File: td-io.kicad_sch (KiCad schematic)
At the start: 12 parts, among them J1 Conn_01x04, J2 USB_B, J3 Conn_01x02, J4 Conn_01x02, Q1 AO4818B, U12 CPC1017N, U2 ISL3175EIBZ-T

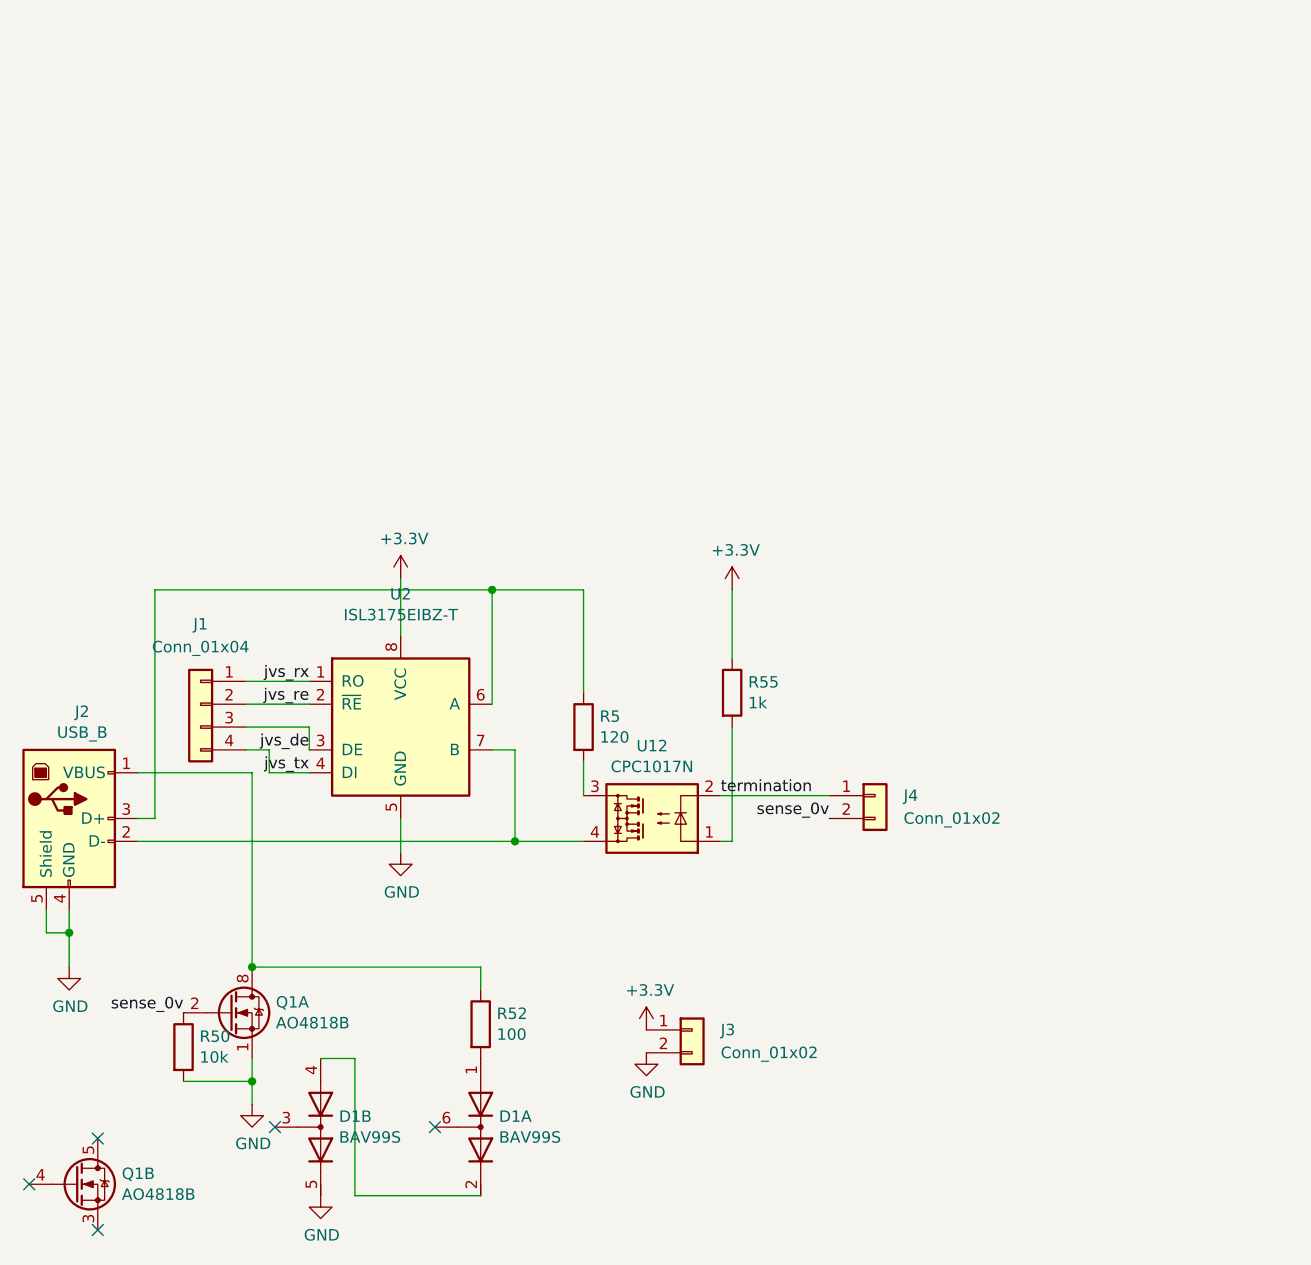
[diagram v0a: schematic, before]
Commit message: Updated pcb with onboard pico
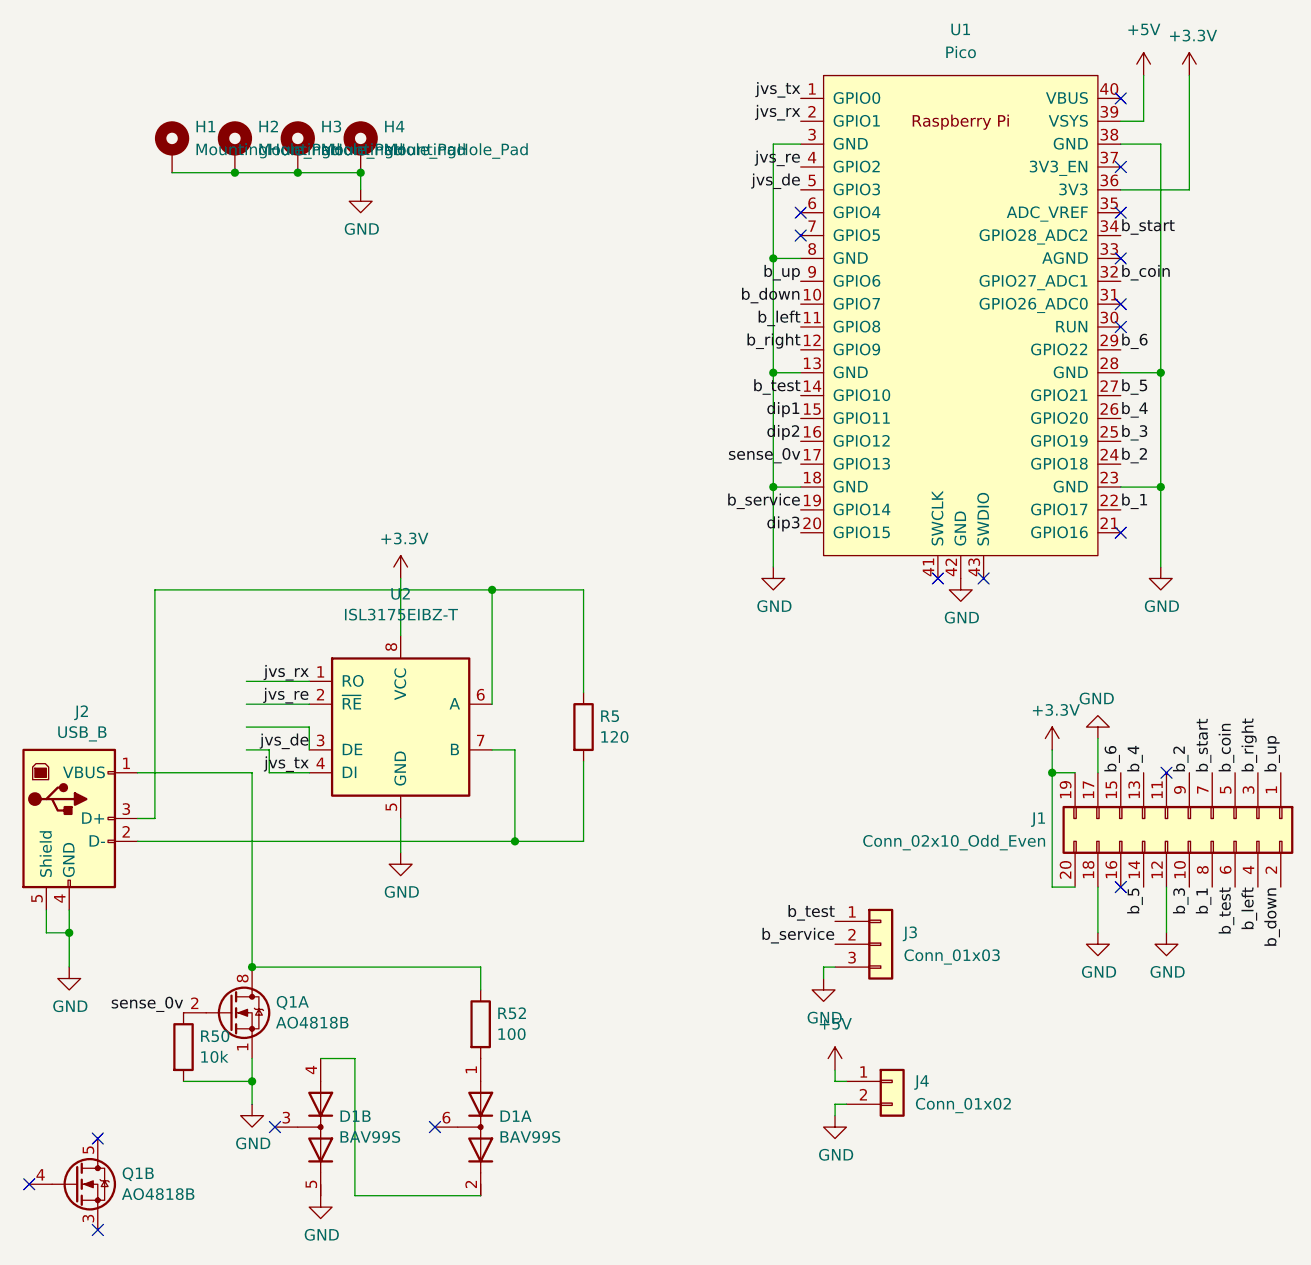
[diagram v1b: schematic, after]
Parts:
- removed J1: Conn_01x04, Connector_PinHeader_2.54mm:PinHeader_1x04_P2.54mm_Vertical, symbol Connector_Generic:Conn_01x04
- removed J3: Conn_01x02, Connector_PinHeader_2.54mm:PinHeader_1x02_P2.54mm_Vertical, symbol Connector_Generic:Conn_01x02
- removed R55: 1k, Resistor_SMD:R_0805_2012Metric, symbol Device:R
- removed U12: CPC1017N, Package_SO:SOP-4_3.8x4.1mm_P2.54mm, symbol Relay_SolidState:CPC1017N
- added H1, H2, H3, H4: MountingHole_Pad, MountingHole:MountingHole_3.5mm_Pad, symbol Mechanical:MountingHole_Pad
- added J1: Conn_02x10_Odd_Even, Connector_PinHeader_2.54mm:PinHeader_2x10_P2.54mm_Vertical, symbol Connector_Generic:Conn_02x10_Odd_Even
- added J3: Conn_01x03, Connector_PinHeader_2.54mm:PinHeader_1x03_P2.54mm_Vertical, symbol Connector_Generic:Conn_01x03
- added U1: Pico, RPi_Pico:RPi_Pico_SMD_TH, symbol MCU_RaspberryPi_and_Boards:Pico
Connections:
- net +3V3: now also J1.19 (Pin_19), J1.20 (Pin_20), U1.36 (3V3)
- net GND: now also J4.2 (Pin_2), H1.1, H2.1, H3.1, H4.1, J1.12 (Pin_12), J1.17 (Pin_17), J1.18 (Pin_18), J3.3 (Pin_3), U1.13 (GND), U1.18 (GND), U1.23 (GND), U1.28 (GND), U1.3 (GND), U1.38 (GND), U1.42 (GND), U1.8 (GND)
- net jvs_de: now also U1.5 (GPIO3)
- net jvs_re: now also U1.4 (GPIO2)
- net jvs_rx: now also U1.2 (GPIO1)
- net jvs_tx: now also U1.1 (GPIO0)
- net sense_0v: now also U1.17 (GPIO13); no longer J4.2 (Pin_2)
- net at J2.2 (D-), U2.7 (B): now also R5.2
- net termination renamed +5V
- net +5V: now also U1.39 (VSYS)
- new net b_1: J1.8 (Pin_8), U1.22 (GPIO17)
- new net b_2: J1.9 (Pin_9), U1.24 (GPIO18)
- new net b_3: J1.10 (Pin_10), U1.25 (GPIO19)
- new net b_4: J1.13 (Pin_13), U1.26 (GPIO20)
- new net b_5: J1.14 (Pin_14), U1.27 (GPIO21)
- new net b_6: J1.15 (Pin_15), U1.29 (GPIO22)
- new net b_coin: J1.5 (Pin_5), U1.32 (GPIO27_ADC1)
- new net b_down: J1.2 (Pin_2), U1.10 (GPIO7)
- new net b_left: J1.4 (Pin_4), U1.11 (GPIO8)
- new net b_right: J1.3 (Pin_3), U1.12 (GPIO9)
- new net b_service: J3.2 (Pin_2), U1.19 (GPIO14)
- new net b_start: J1.7 (Pin_7), U1.34 (GPIO28_ADC2)
- new net b_test: J1.6 (Pin_6), J3.1 (Pin_1), U1.14 (GPIO10)
- new net b_up: J1.1 (Pin_1), U1.9 (GPIO6)
- new net dip1: U1.15 (GPIO11)
- new net dip2: U1.16 (GPIO12)
- new net dip3: U1.20 (GPIO15)
- no-connect marks 5 -> 18

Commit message: Add some breakout pins
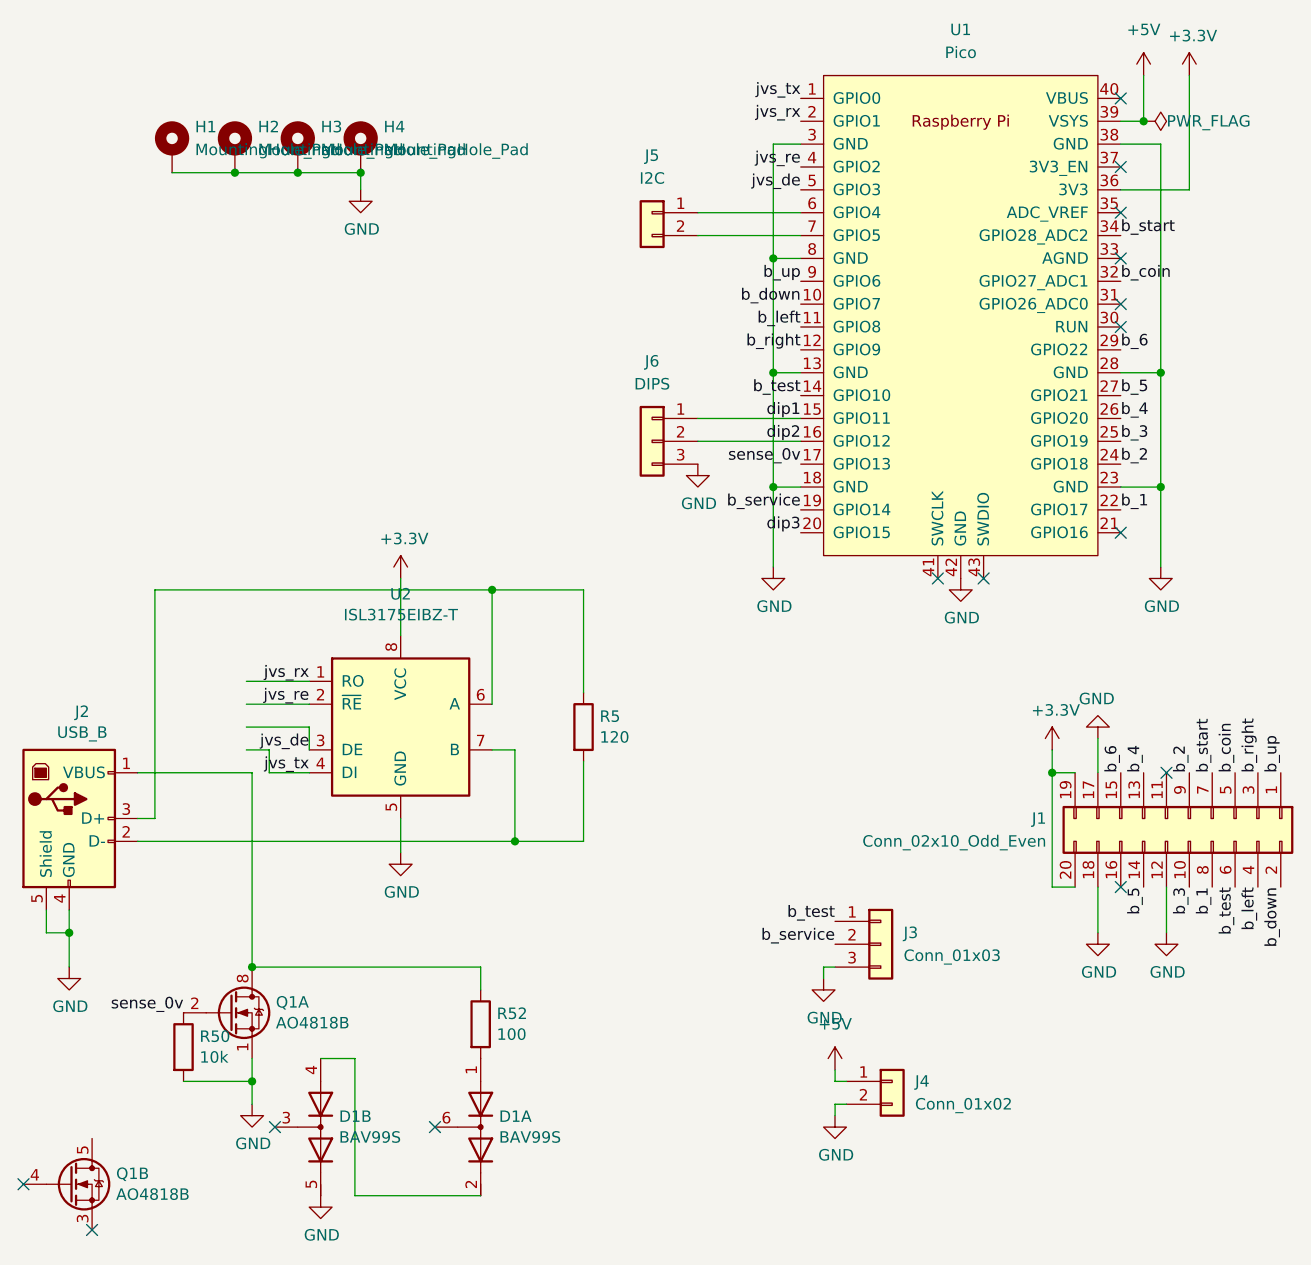
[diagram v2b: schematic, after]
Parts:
- added J5: I2C, Connector_PinHeader_2.54mm:PinHeader_1x02_P2.54mm_Vertical, symbol Connector_Generic:Conn_01x02
- added J6: DIPS, Connector_PinHeader_2.54mm:PinHeader_1x03_P2.54mm_Vertical, symbol Connector_Generic:Conn_01x03
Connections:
- net GND: now also J6.3 (Pin_3)
- net dip1: now also J6.1 (Pin_1)
- net dip2: now also J6.2 (Pin_2)
- net at U1.6 (GPIO4): now also J5.1 (Pin_1)
- net at U1.7 (GPIO5): now also J5.2 (Pin_2)
- no-connect marks 18 -> 15
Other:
- moved on the sheet: Q1B
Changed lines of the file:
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@@
   (junction (at 264.795 88.265) (diameter 0) (color 0 0 0 0)
+  )
+  (junction (at 365.76 82.55) (diameter 0) (color 0 0 0 0)
   )
   (junction (at 367.665 123.19) (diameter 0) (color 0 0 0 0)
@@
   (no_connect (at 269.24 194.31))
   (no_connect (at 363.22 102.87))
-  (no_connect (at 241.935 200.66))
-  (no_connect (at 249.555 205.74))
+  (no_connect (at 241.3 200.66))
+  (no_connect (at 248.92 205.74))
   (no_connect (at 347.98 133.35))
   (no_connect (at 342.9 133.35))
-  (no_connect (at 249.555 195.58))
   (no_connect (at 363.22 128.27))
-  (no_connect (at 327.66 95.25))
-  (no_connect (at 327.66 92.71))
   (wire (pts (xy 283.21 160.02) (xy 283.21 163.83))
     (stroke (width 0) (type default) (color 0 0 0 0))
   )
+  (wire (pts (xy 316.23 115.57) (xy 327.66 115.57))
+    (stroke (width 0) (type default) (color 0 0 0 0))
+  )
   (wire (pts (xy 292.1 176.53) (xy 292.1 179.07))
     (stroke (width 0) (type default) (color 0 0 0 0))
@@
     (stroke (width 0) (type default) (color 0 0 0 0))
   )
+  (wire (pts (xy 316.23 95.25) (xy 327.66 95.25))
+    (stroke (width 0) (type default) (color 0 0 0 0))
+  )
   (wire (pts (xy 332.74 191.77) (xy 331.47 191.77))
     (stroke (width 0) (type default) (color 0 0 0 0))
   )
+  (wire (pts (xy 316.23 118.11) (xy 327.66 118.11))
+    (stroke (width 0) (type default) (color 0 0 0 0))
+  )
   (wire (pts (xy 243.84 170.18) (xy 243.84 172.72))
     (stroke (width 0) (type default) (color 0 0 0 0))
@@
   )
   (wire (pts (xy 278.13 186.69) (xy 274.32 186.69))
+    (stroke (width 0) (type default) (color 0 0 0 0))
+  )
+  (wire (pts (xy 316.23 92.71) (xy 327.66 92.71))
     (stroke (width 0) (type default) (color 0 0 0 0))
   )
@@
     (pin "1")
   )
-  (symbol (lib_id "Transistor_FET:FDS6930B") (at 247.015 200.66 0) (unit 2)
-    (in_bom yes) (on_board yes)
-    (property "Reference" "Q1" (id 0) (at 252.222 199.4916 0)
-      (effects (font (size 1.27 1.27)) (justify left))
-    )
-    (property "Value" "AO4818B" (id 1) (at 252.222 201.803 0)
-      (effects (font (size 1.27 1.27)) (justify left))
-    )
-    (property "Footprint" "Package_SO:SOIC-8_3.9x4.9mm_P1.27mm" (id 2) (at 252.095 202.565 0)
+  (symbol (lib_id "Transistor_FET:FDS6930B") (at 246.38 200.66 0) (unit 2)
+    (in_bom yes) (on_board yes)
+    (property "Reference" "Q1" (id 0) (at 251.587 199.4916 0)
+      (effects (font (size 1.27 1.27)) (justify left))
+    )
+    (property "Value" "AO4818B" (id 1) (at 251.587 201.803 0)
+      (effects (font (size 1.27 1.27)) (justify left))
+    )
+    (property "Footprint" "Package_SO:SOIC-8_3.9x4.9mm_P1.27mm" (id 2) (at 251.46 202.565 0)
       (effects (font (size 1.27 1.27) italic) (justify left) hide)
     )
-    (property "Datasheet" "http://www.onsemi.com/pub/Collateral/FDS6930B-D.PDF" (id 3) (at 247.015 200.66 0)
+    (property "Datasheet" "http://www.onsemi.com/pub/Collateral/FDS6930B-D.PDF" (id 3) (at 246.38 200.66 0)
       (effects (font (size 1.27 1.27)) (justify left) hide)
     )
-    (property "Digikey" "785-1059-1-ND" (id 4) (at 247.015 200.66 0)
+    (property "Digikey" "785-1059-1-ND" (id 4) (at 246.38 200.66 0)
       (effects (font (size 1.27 1.27)) hide)
     )
@@
     )
     (pin "1")
+  )
+  (symbol (lib_id "Connector_Generic:Conn_01x03") (at 311.15 118.11 0) (mirror y) (unit 1)
+    (in_bom yes) (on_board yes) (fields_autoplaced)
+    (property "Reference" "J6" (id 0) (at 311.15 109.22 0))
+    (property "Value" "DIPS" (id 1) (at 311.15 111.76 0))
+    (property "Footprint" "Connector_PinHeader_2.54mm:PinHeader_1x03_P2.54mm_Vertical" (id 2) (at 311.15 118.11 0)
+      (effects (font (size 1.27 1.27)) hide)
+    )
+    (property "Datasheet" "~" (id 3) (at 311.15 118.11 0)
+      (effects (font (size 1.27 1.27)) hide)
+    )
+    (pin "1")
+    (pin "2")
+    (pin "3")
   )
   (symbol (lib_id "power:GND") (at 324.612 132.08 0) (unit 1)
@@
     (pin "1")
   )
+  (symbol (lib_id "power:GND") (at 316.23 120.65 0) (unit 1)
+    (in_bom yes) (on_board yes)
+    (property "Reference" "#PWR0117" (id 0) (at 316.23 127 0)
+      (effects (font (size 1.27 1.27)) hide)
+    )
+    (property "Value" "GND" (id 1) (at 316.357 125.0442 0))
+    (property "Footprint" "" (id 2) (at 316.23 120.65 0)
+      (effects (font (size 1.27 1.27)) hide)
+    )
+    (property "Datasheet" "" (id 3) (at 316.23 120.65 0)
+      (effects (font (size 1.27 1.27)) hide)
+    )
+    (pin "1")
+  )
   (symbol (lib_id "Connector_Generic:Conn_01x03") (at 336.55 173.99 0) (unit 1)
     (in_bom yes) (on_board yes) (fields_autoplaced)
@@
     )
     (property "Datasheet" "~" (id 3) (at 264.795 85.725 0)
+      (effects (font (size 1.27 1.27)) hide)
+    )
+    (pin "1")
+  )
+  (symbol (lib_id "power:PWR_FLAG") (at 365.76 82.55 270) (unit 1)
+    (in_bom yes) (on_board yes)
+    (property "Reference" "#FLG0101" (id 0) (at 367.665 82.55 0)
+      (effects (font (size 1.27 1.27)) hide)
+    )
+    (property "Value" "PWR_FLAG" (id 1) (at 368.3 82.55 90)
+      (effects (font (size 1.27 1.27)) (justify left))
+    )
+    (property "Footprint" "" (id 2) (at 365.76 82.55 0)
+      (effects (font (size 1.27 1.27)) hide)
+    )
+    (property "Datasheet" "~" (id 3) (at 365.76 82.55 0)
       (effects (font (size 1.27 1.27)) hide)
     )
@@
     (pin "9")
   )
+  (symbol (lib_id "Connector_Generic:Conn_01x02") (at 311.15 92.71 0) (mirror y) (unit 1)
+    (in_bom yes) (on_board yes) (fields_autoplaced)
+    (property "Reference" "J5" (id 0) (at 311.15 86.36 0))
+    (property "Value" "I2C" (id 1) (at 311.15 88.9 0))
+    (property "Footprint" "Connector_PinHeader_2.54mm:PinHeader_1x02_P2.54mm_Vertical" (id 2) (at 311.15 92.71 0)
+      (effects (font (size 1.27 1.27)) hide)
+    )
+    (property "Datasheet" "~" (id 3) (at 311.15 92.71 0)
+      (effects (font (size 1.27 1.27)) hide)
+    )
+    (pin "1")
+    (pin "2")
+  )
   (symbol (lib_id "Connector_Generic:Conn_01x02") (at 337.82 189.23 0) (unit 1)
     (in_bom yes) (on_board yes) (fields_autoplaced)
@@
   )
   (symbol_instances
+    (path "/b452654c-0af9-452a-9138-4303c0e3ebb7"
+      (reference "#FLG0101") (unit 1) (value "PWR_FLAG") (footprint "")
+    )
     (path "/0e2f4b55-afcf-4e5f-9559-8b2ad2098638"
       (reference "#PWR0101") (unit 1) (value "GND") (footprint "")
@@
       (reference "#PWR0116") (unit 1) (value "GND") (footprint "")
     )
+    (path "/887d0669-7224-46c3-b959-0cacd5c8d6af"
+      (reference "#PWR0117") (unit 1) (value "GND") (footprint "")
+    )
     (path "/00000000-0000-0000-0000-0000610da9f2"
       (reference "#PWR0139") (unit 1) (value "GND") (footprint "")
@@
       (reference "J4") (unit 1) (value "Conn_01x02") (footprint "Connector_PinHeader_2.54mm:PinHeader_1x02_P2.54mm_Vertical")
     )
+    (path "/be813dec-c91f-4c06-808b-c742fd6baf99"
+      (reference "J5") (unit 1) (value "I2C") (footprint "Connector_PinHeader_2.54mm:PinHeader_1x02_P2.54mm_Vertical")
+    )
+    (path "/37ca6a20-f162-4f7d-b75b-aebcef62a374"
+      (reference "J6") (unit 1) (value "DIPS") (footprint "Connector_PinHeader_2.54mm:PinHeader_1x03_P2.54mm_Vertical")
+    )
     (path "/00000000-0000-0000-0000-000060ff630d"
